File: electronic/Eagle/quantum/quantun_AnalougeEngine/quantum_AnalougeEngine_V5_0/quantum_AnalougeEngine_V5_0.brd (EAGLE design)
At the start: 200 x 80 mm, 195 parts, among them IC1 OP275, IC10 STM32F767ZIT6, IC2 DAC084S085CIMM_NOPB, IC3 DAC084S085CIMM_NOPB, IC4 OP275, IC5 OP275, IC6 LAN8742A-CZ-TR, IC7 TL072, IC8 OP275, IC9 TL072, J1 GWLEX-SMT-S988G_Y, K1 K1, K2 K2, K3 K3, K4 K4, K5 K5, K6 K6, K7 K7, K8 K8, T1 H1102NL, U12 ULN2003, U2 7812, U4 THAT1240, U6 THAT1240, U7 THAT1240, U8 THAT1240

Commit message: continue on AnalougeEngine_V_5_0
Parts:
- removed C44: 10 µF, C_Sager_Bibliothek:CAPAE400X550N
- added C41: (no value), passive components:C0603
- added C42, C51, C64: 10 uF, passive components:C1206
- added C52, C59: 1 uF, passive components:C0603
- added CON3: (no value), electro_mechanical:87832-10
- added IC11: AD7606BSTZ, C_Sager_Bibliothek:QFP50P1200X1200X160-64N
- added R14, R29: 10k, C_Sager_Bibliothek:R0603
- C31, C32, C33, C34: value 10 µF -> 10 uF; device C_Sager_Bibliothek:CAPAE400X550N -> passive components:C1206
- R10, R11, R12, R33, R34, R7, R8, R9: value 470R -> 680R
- R35: value 0R -> 10k
- moved R35 59.4 mm to (148.4, 49.0), turned to 0 degrees
- moved S1 51.9 mm to (131.4, 9.90)
- moved R60 45.2 mm to (104.1, 35.5)
- moved R15 24.9 mm to (78.2, 13.4)
- moved R16 24.9 mm to (78.2, 11.9)
- moved R21 24.9 mm to (81.4, 6.10)
- moved R22 24.9 mm to (81.4, 4.60)
- moved R23 24.9 mm to (78.2, 10.3)
- moved R24 24.9 mm to (78.2, 8.90)
- moved R25 24.9 mm to (78.2, 7.50)
- moved R6 24.9 mm to (78.2, 14.9)
- moved R13 24.9 mm to (81.3, 13.4)
- moved R17 24.9 mm to (81.3, 11.9)
- moved R18 24.9 mm to (81.3, 10.3)
- moved R19 24.9 mm to (81.3, 8.90)
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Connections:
- removed net +3V3_STM32: R1.2
- new net +5V_DIGITAL: C41.1, IC11.23, IC11.37, IC11.38, IC11.48, R1.2, R29.2, R35.1
- new net BUSY: IC11.14
- new net CS: IC11.13
- new net CV_A_B: IC11.10, IC11.9
- new net DB0: IC11.16
- new net DB1: IC11.17
- new net DB10: IC11.28
- new net DB11: IC11.29
- new net DB12: IC11.30
- new net DB13: IC11.31
- new net DB14: IC11.32
- new net DB15: IC11.33
- new net DB2: IC11.18
- new net DB3: IC11.19
- new net DB4: IC11.20
- new net DB5: IC11.21
- new net DB6: IC11.22
- new net DB7: IC11.24
- new net DB8: IC11.25
- new net DB9: IC11.27
- new net FRST: IC11.15
- new net N$37: R77.2, TP05.P$1
- new net N$38: IC11.6, R14.1, R29.1
- new net N$39: IC11.34, R35.2
- new net N$40: C42.1, IC11.44, IC11.45
- new net N$41: C51.1, IC11.42
- new net N$42: C52.1, IC11.36
- new net N$44: C59.1, IC11.39
- new net OS0: IC11.3
- new net OS1: IC11.4
- new net OS2: IC11.5
- new net RANGE: IC11.8
- new net RD: IC11.12
- new net RESET: IC11.11
- net +5V_STM32: now also C33.1; no longer C44.1
- net 1V_DAC: now also C64.1; no longer C33.1
- net AGND: now also C41.2, C42.2, C51.2, C52.2, C59.2, C64.2, C69.2, C70.2, IC11.26, IC11.40, IC11.41, IC11.43, IC11.46, IC11.47, IC11.50, IC11.52, IC11.54, IC11.56, IC11.58, IC11.60, IC11.62, IC11.64, R14.2, U12.8, U2.2; no longer C33.2, R35.1
- net DGND: now also C33.2; no longer C44.2, C69.2, C70.2, R35.2, R77.2, TP05.P$1, U12.8, U2.2
- net N$10: now also IC11.53
- net N$12: now also IC11.55
- net N$20: now also IC11.57
- net N$34: now also IC11.59
- net N$35: now also IC11.61
- net N$36: now also IC11.63
- net N$4: now also IC11.49
- net N$6: now also IC11.51
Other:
- outline, holes or cut-outs redrawn

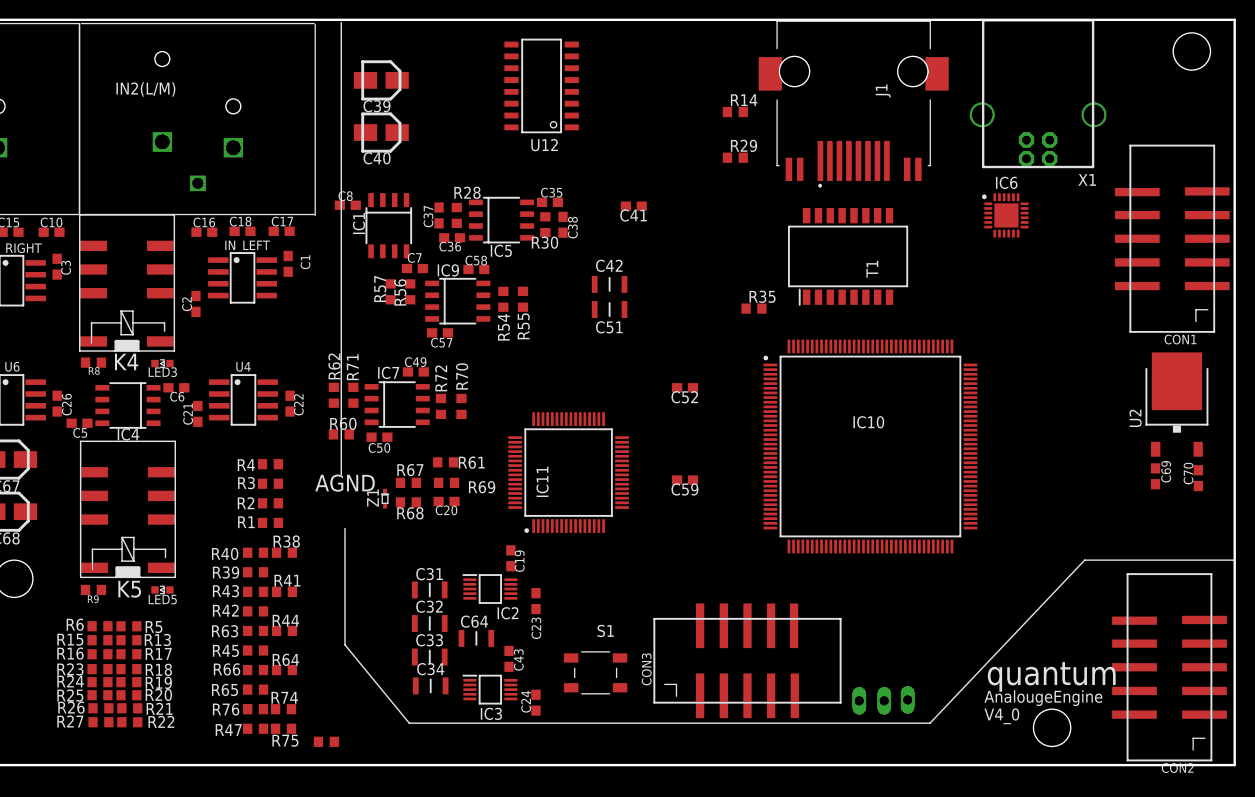
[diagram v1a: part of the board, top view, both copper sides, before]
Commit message: Continued on "AnlougeEngine_V_5_0" - Changed little timing in ADC read. Changed left/right send to FrontDisplay
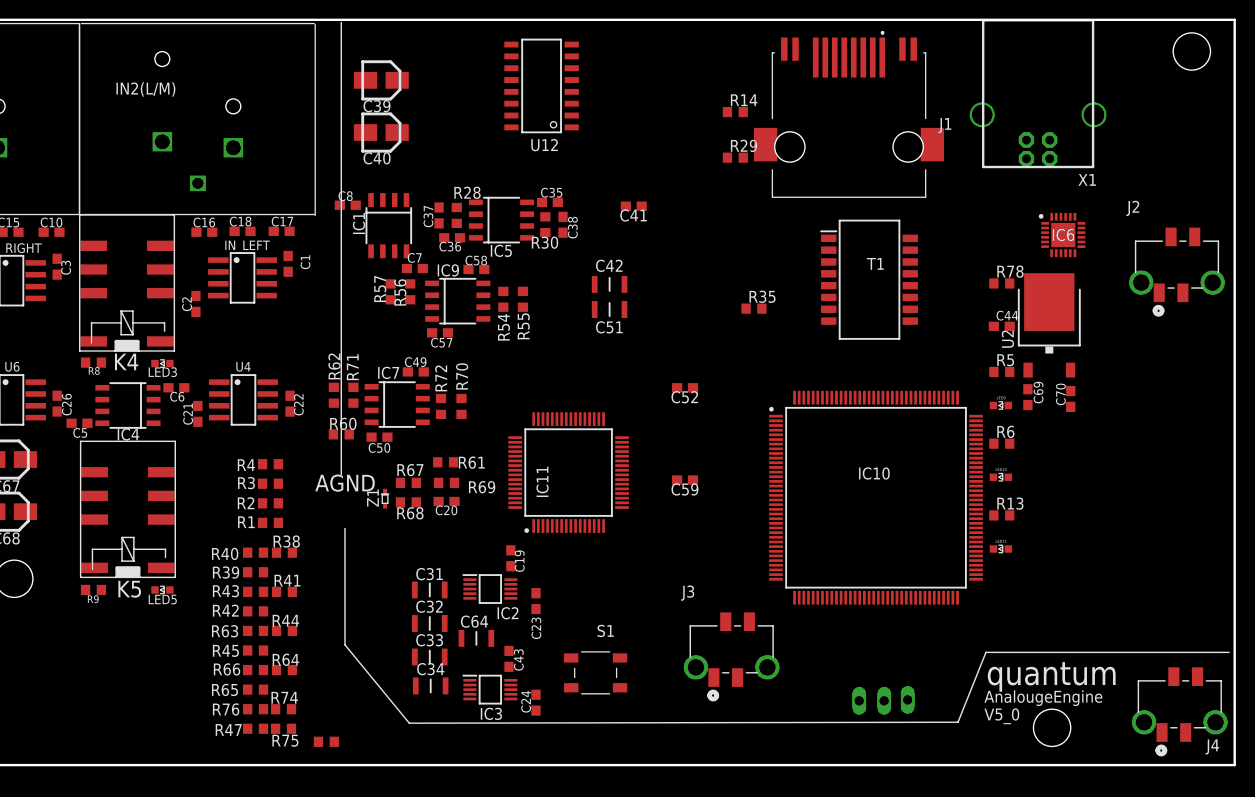
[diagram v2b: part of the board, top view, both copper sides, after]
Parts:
- removed CON1, CON2, CON3: (no value), electro_mechanical:87832-10
- removed R15, R16, R17, R18, R19, R20, R21, R22, R23, R24, R25, R26, R27: 10k, C_Sager_Bibliothek:R0603
- added C44: 100nF, C_Sager_Bibliothek:C0603
- added J2, J3, J4: 90814-0204, electro_mechanical:MOLEX_90814-0204
- added LED10, LED11, LED9: LED_BLUE_SMD, C_Sager_Bibliothek:WL-SMCW_0603
- added R78: 10 k, C_Sager_Bibliothek:R0603
- C41: value (none) -> 100 nF
- R13, R5, R6: value 10k -> 680R
- moved R6 98.8 mm to (175.0, 34.5)
- moved R5 97.6 mm to (175.0, 42.2), turned to 0 degrees
- moved R13 94.7 mm to (175.0, 26.8), turned to 0 degrees
- moved U2 16.1 mm to (180.1, 47.2)
- moved C69 16.1 mm to (177.8, 39.5)
- moved C70 16.1 mm to (182.4, 39.3)
- moved IC6 6.45 mm to (181.6, 56.9)
- moved IC10 5.53 mm to (161.5, 28.7)
- moved T1 3.40 mm to (160.8, 52.1), turned to 0 degrees
- moved J1 3.04 mm to (158.6, 68.9), turned to 0 degrees
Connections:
- removed net N$10: IC11.53, R16.2, R17.2
- removed net N$20: IC11.57, R19.2, R24.2
- removed net N$35: IC11.61, R21.2, R26.2
- removed net N$36: IC11.63, R22.2, R27.2
- removed net N$46: R21.1
- new net DEBUG1: IC10.21
- new net DEBUG2: IC10.115
- new net LD1: IC10.46, LED9.2
- new net LD2: IC10.137, LED10.2
- new net LD3: IC10.75, LED11.2
- new net N$100: IC10.27
- new net N$101: IC10.28
- new net N$103: IC10.30
- new net N$104: IC10.31
- new net N$105: IC10.32
- new net N$106: IC10.33
- new net N$107: IC10.34
- new net N$108: IC10.35
- new net N$109: IC10.36
- new net N$110: IC10.37
- new net N$111: IC10.38
- new net N$112: IC10.39
- new net N$115: IC10.42
- new net N$116: IC10.43
- new net N$117: IC10.44
- new net N$118: IC10.45
- new net N$120: IC10.47
- new net N$121: IC10.48
- new net N$122: IC10.49
- new net N$123: IC10.50
- new net N$124: IC10.51
- new net N$125: IC10.52
- new net N$126: IC10.53
- new net N$127: IC10.54
- new net N$128: IC10.55
- new net N$134: IC10.61
- new net N$135: IC10.62
- new net N$143: IC10.70
- new net N$144: IC10.71
- new net N$145: IC10.72
- new net N$146: IC10.108
- new net N$147: IC10.107
- new net N$148: IC10.106
- new net N$150: IC10.104
- new net N$151: IC10.103
- new net N$152: IC10.102
- new net N$153: IC10.101
- new net N$154: IC10.100
- new net N$159: IC10.95
- new net N$160: IC10.94
- new net N$161: IC10.93
- new net N$162: IC10.92
- new net N$163: IC10.91
- new net N$164: IC10.90
- new net N$165: IC10.89
- new net N$168: IC10.86
- new net N$169: IC10.85
- new net N$170: IC10.84
- new net N$171: IC10.83
- new net N$172: IC10.82
- new net N$173: IC10.81
- new net N$174: IC10.80
- new net N$175: IC10.79
- new net N$178: IC10.76
- new net N$180: IC10.74
- new net N$181: IC10.73
- new net N$182: IC10.144
- new net N$183: IC10.143
- new net N$186: IC10.140
- new net N$187: IC10.139
- new net N$188: IC10.138, R78.1
- new net N$190: IC10.136
- new net N$193: IC10.133
- new net N$195: IC10.131
- new net N$196: IC10.130
- new net N$197: IC10.129
- new net N$198: IC10.128
- new net N$200: IC10.126
- new net N$205: IC10.121
- new net N$206: IC10.120
- new net N$207: IC10.119
- new net N$208: IC10.118
- new net N$209: IC10.117
- new net N$212: IC10.114
- new net N$216: IC10.110
- new net N$69: IC10.6
- new net N$70: IC10.7
- new net N$76: IC10.8
- new net N$82: IC10.9
- new net N$83: IC10.10
- new net N$84: IC10.11
- new net N$85: IC10.12
- new net N$86: IC10.13
- new net N$87: IC10.14
- new net N$88: IC10.15
- new net N$89: IC10.16
- new net N$90: IC10.17
- new net N$91: IC10.18
- new net N$92: IC10.19
- new net N$93: IC10.20
- new net N$95: IC10.22
- new net N$96: IC10.23
- new net N$97: IC10.24
- new net N$99: IC10.26
- new net NRST: C44.2, IC10.25, J4.2, S1.3, S1.4
- new net SWCLK: IC10.109, J4.1
- new net SWDIO: IC10.105, J4.3
- new net USART3_RX: IC10.77
- new net USART3_TX: IC10.78
- new net USART6_RX: IC10.96
- new net USART6_TX: IC10.97
- net AGND: now also C44.1, J4.4, R13.1, R5.1, R78.2, S1.1, S1.2; no longer R15.1, R16.1, R23.1, R24.1, R25.1, R26.1, R27.1
- net BUSY: now also IC10.88
- net CS: now also IC10.123
- net CS_DAC1: now also IC10.134
- net CS_DAC2: now also IC10.135
- net CV_A_B: now also IC10.113
- net DAC_OUT1: now also IC10.40
- net DAC_OUT2: now also IC10.41
- net DB0: now also IC10.141
- net DB1: now also IC10.142
- net DB10: now also IC10.63
- net DB11: now also IC10.64
- net DB12: now also IC10.65
- net DB13: now also IC10.66
- net DB14: now also IC10.67
- net DB15: now also IC10.68
- net DB2: now also IC10.1
- net DB3: now also IC10.2
- net DB4: now also IC10.3
- net DB5: now also IC10.4
- net DB6: now also IC10.5
- net DB7: now also IC10.58
- net DB8: now also IC10.59
- net DB9: now also IC10.60
- net DIN_DAC: now also IC10.29
- net FRST: now also IC10.122
- net L/M_IN(VCA1_IN): now also IC11.49; no longer R5.1
- net L/M_OUT(OUT_STAGE_LEFT): now also IC11.57; no longer R19.1
- net L/M_OUT(VCA1_OUT): now also IC11.53; no longer R17.1
- net N$12: now also LED10.1, R6.2; no longer IC11.55, R18.2, R23.2
- net N$34: now also LED11.1, R13.2; no longer IC11.59, R20.2, R25.2
- net N$4: now also IC11.61; no longer IC11.49, R5.2, R6.2
- net N$47: now also IC11.63; no longer R22.1
- net N$6: now also LED9.1, R5.2; no longer IC11.51, R13.2, R15.2
- net OS0: now also IC10.98
- net OS1: now also IC10.99
- net OS2: now also IC10.111
- net R/S_IN(VCA2_IN): now also IC11.51; no longer R13.1
- net R/S_OUT(OUT_STAGE_RIGHT): now also IC11.59; no longer R20.1
- net R/S_OUT(VCA2_OUT): now also IC11.55; no longer R18.1
- net RANGE: now also IC10.112
- net RD: now also IC10.116
- net RELAIS1: now also IC10.57
- net RELAIS2: now also IC10.56
- net RELAIS3: now also IC10.132
- net RELAIS4: now also IC10.125
- net RELAIS5: now also IC10.127
- net RELAIS6: now also IC10.124
- net RESET: now also IC10.87
- net SCLK_DAC: now also IC10.69
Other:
- board text added: "AnalougeEngine V5_0"
- board text removed: "AnalougeEngine V4_0"

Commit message: progess on Analouge Engine V_5_0
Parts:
- removed C69: 0.33 uF, C_Sager_Bibliothek:C0603
- removed C70: 100 nF, C_Sager_Bibliothek:C0603
- removed J3, J4: 90814-0204, electro_mechanical:MOLEX_90814-0204
- removed R77: 0R, C_Sager_Bibliothek:R0603
- removed TP03, TP05, TP06: TPTHT, C_Sager_Bibliothek:THT_PIN
- removed U2: 7812, C_Sager_Bibliothek:TO252
- added ANALOGVOLT, PROG.: 90814-0204, electro_mechanical:MOLEX_90814-0204
- added DEBUG1, DEBUG2, TP04: TPTHT, C_Sager_Bibliothek:THT_PIN
- added IC12: ESDA6V1BC6, NUCLEO_parts:SOT95P280X145-6N
- added R15, R16, R17: 0R, C_Sager_Bibliothek:R0603
- added R18, R19: 10 k, C_Sager_Bibliothek:R0603
- moved R14 12.1 mm to (134.3, 71.1)
- moved R29 12.1 mm to (134.3, 66.2)
- moved J1 7.75 mm to (151.5, 72.0), turned to 180 degrees
- moved IC10 4.47 mm to (157.5, 26.7)
- moved IC6 0.95 mm to (182.5, 57.2)
- renumbered J2 to DIG_VOLT
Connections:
- net N$100 renamed RMII_MDC
- net N$108 renamed RMII_REF_CLK
- net N$109 renamed RMII_MDIO
- net N$116 renamed RMSII_CRS_DV
- net N$117 renamed RMII_RXD0
- net N$118 renamed RMII_RXD1
- net N$15 renamed NEGATIVE_OUT(L/M)
- net N$152 renamed USB_ID
- net N$17 renamed POSITIVE_OUT(L/M)
- net N$180 renamed RMII_TXD1
- net N$188 renamed BOOT0
- net N$198 renamed RMII_TXD0
- net N$200 renamed RMII_TX_EN
- net N$21 renamed POSITIVE_IN(R/S)
- net N$22 renamed NEGATIVE_IN(R/S)
- net N$23 renamed POSITIVE_OUT(R/S)
- net N$24 renamed NGATIVE_OUT(R/S)
- net N$25 renamed NEGATIVE_IN(L/M)
- net N$27 renamed POSITIVE_IN(L/M)
- removed net +5V_STM32: C19.1, C31.1, C33.1, C43.1, IC2.1, IC3.1
- removed net BOTTOM: TP06.P$1
- removed net N$101: IC10.28
- removed net N$103: IC10.30
- removed net N$104: IC10.31
- removed net N$105: IC10.32
- removed net N$106: IC10.33
- removed net N$107: IC10.34
- removed net N$110: IC10.37
- removed net N$111: IC10.38
- removed net N$112: IC10.39
- removed net N$115: IC10.42
- removed net N$120: IC10.47
- removed net N$121: IC10.48
- removed net N$122: IC10.49
- removed net N$123: IC10.50
- removed net N$124: IC10.51
- removed net N$125: IC10.52
- removed net N$126: IC10.53
- removed net N$127: IC10.54
- removed net N$128: IC10.55
- removed net N$134: IC10.61
- removed net N$135: IC10.62
- removed net N$143: IC10.70
- removed net N$144: IC10.71
- removed net N$145: IC10.72
- removed net N$146: IC10.108
- removed net N$147: IC10.107
- removed net N$148: IC10.106
- removed net N$150: IC10.104
- removed net N$151: IC10.103
- removed net N$153: IC10.101
- removed net N$154: IC10.100
- removed net N$159: IC10.95
- removed net N$160: IC10.94
- removed net N$161: IC10.93
- removed net N$162: IC10.92
- removed net N$163: IC10.91
- removed net N$164: IC10.90
- removed net N$165: IC10.89
- removed net N$168: IC10.86
- removed net N$169: IC10.85
- removed net N$170: IC10.84
- removed net N$171: IC10.83
- removed net N$172: IC10.82
- removed net N$173: IC10.81
- removed net N$174: IC10.80
- removed net N$175: IC10.79
- removed net N$178: IC10.76
- removed net N$181: IC10.73
- removed net N$182: IC10.144
- removed net N$183: IC10.143
- removed net N$186: IC10.140
- removed net N$187: IC10.139
- removed net N$190: IC10.136
- removed net N$193: IC10.133
- removed net N$195: IC10.131
- removed net N$196: IC10.130
- removed net N$197: IC10.129
- removed net N$205: IC10.121
- removed net N$206: IC10.120
- removed net N$207: IC10.119
- removed net N$208: IC10.118
- removed net N$209: IC10.117
- removed net N$212: IC10.114
- removed net N$37: R77.2, TP05.P$1
- removed net N$69: IC10.6
- removed net N$70: IC10.7
- removed net N$76: IC10.8
- removed net N$82: IC10.9
- removed net N$83: IC10.10
- removed net N$84: IC10.11
- removed net N$85: IC10.12
- removed net N$86: IC10.13
- removed net N$87: IC10.14
- removed net N$88: IC10.15
- removed net N$89: IC10.16
- removed net N$90: IC10.17
- removed net N$91: IC10.18
- removed net N$92: IC10.19
- removed net N$93: IC10.20
- removed net N$95: IC10.22
- removed net N$96: IC10.23
- removed net N$97: IC10.24
- removed net N$99: IC10.26
- new net +3V3: ANALOGVOLT.1
- new net +5V: ANALOGVOLT.4, C19.1, C31.1, C33.1, C41.1, C43.1, IC11.1, IC11.23, IC11.37, IC11.38, IC11.48, IC2.1, IC3.1, R29.2, R35.1
- new net A_GND_TO_STAR: DIG_VOLT.3, R16.1
- new net D_GND_TO_STAR: ANALOGVOLT.3, R15.1
- new net N$10: IC10.101, R19.1
- new net PB2/BOOT1: IC10.48, R18.2
- new net USB_DM: IC10.103, IC12.3, X1.2
- new net USB_DP: IC10.104, IC12.6, X1.3
- new net USB_VBUS: IC12.1, R19.2, X1.1
- net +12V: now also ANALOGVOLT.2; no longer C70.1, U2.3
- net +5V_DIGITAL: no longer C41.1, IC11.23, IC11.37, IC11.38, IC11.48, R29.2, R35.1
- net AGND: now also IC11.2, IC12.2, IC12.5, PROG..4, R15.2, R16.2, R17.2, R18.1, X1.4; no longer C69.2, C70.2, J4.4, U2.2
- net CHASIS: now also R17.1, TP04.P$1; no longer R77.1, TP03.P$1
- net DEBUG1: now also DEBUG1.P$1
- net DEBUG2: now also DEBUG2.P$1
- net L/M_OUT+: now also K3.S2; no longer K3.S1
- net L/M_OUT-: now also K3.S1; no longer K3.S2
- net NRST: now also PROG..2; no longer J4.2
- net R/S_OUT+: now also K2.S2; no longer K2.S1
- net R/S_OUT-: now also K2.S1; no longer K2.S2
- net SWCLK: now also PROG..1; no longer J4.1
- net SWDIO: now also PROG..3; no longer J4.3
- net V+: now also DIG_VOLT.1; no longer C69.1, U2.1
- net V-: now also DIG_VOLT.2
